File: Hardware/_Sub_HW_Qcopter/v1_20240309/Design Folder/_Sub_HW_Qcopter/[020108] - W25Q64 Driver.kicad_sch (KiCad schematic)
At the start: 3 parts, among them U2001 W25Q64JVSSIQ

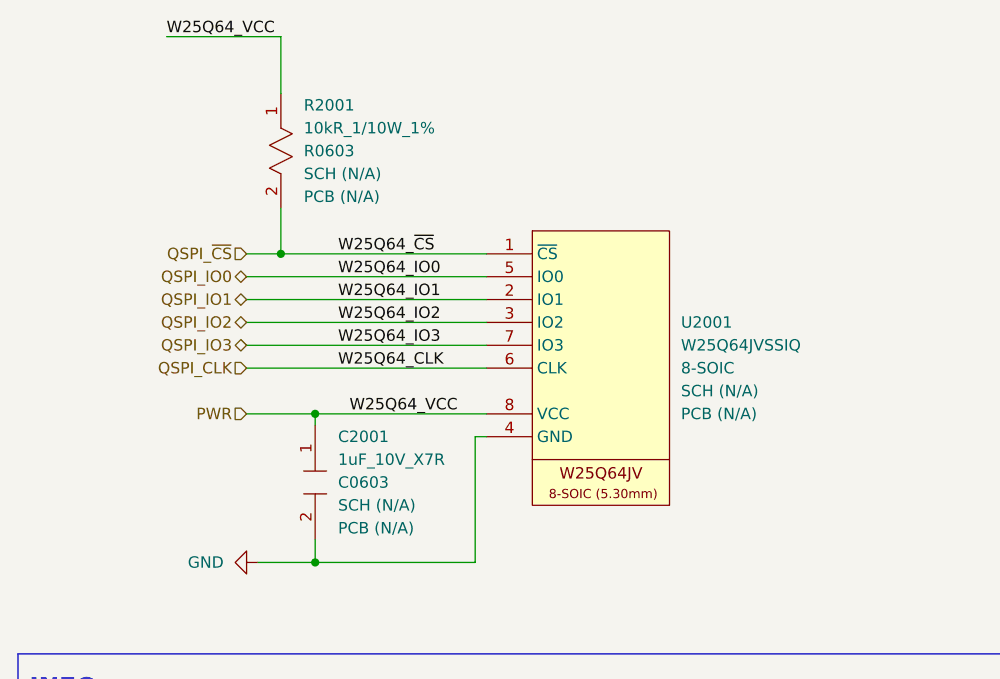
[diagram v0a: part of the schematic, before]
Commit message: Update [020108] - W25Q64 Driver.kicad_sch
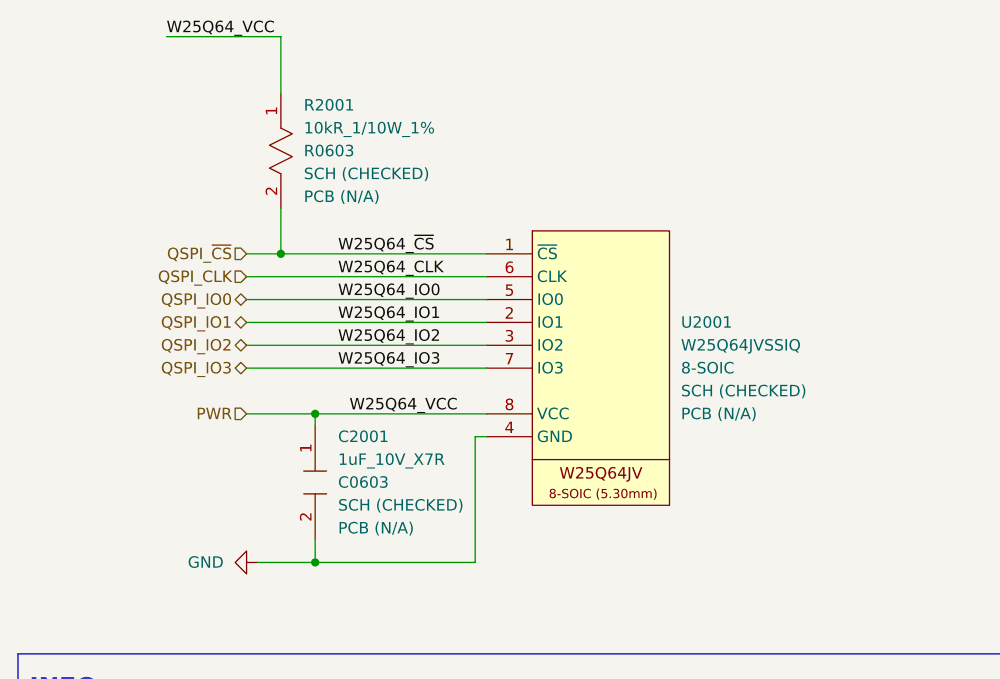
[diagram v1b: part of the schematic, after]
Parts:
- C2001, R2001, U2001: SCH CHECK SCH (N/A) -> SCH (CHECKED)
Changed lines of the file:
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@@
 	(wire
 		(pts
-			(xy 215.9 184.15) (xy 242.57 184.15)
+			(xy 215.9 186.69) (xy 242.57 186.69)
 		)
 		(stroke
@@
 	(wire
 		(pts
-			(xy 215.9 189.23) (xy 242.57 189.23)
+			(xy 215.9 179.07) (xy 242.57 179.07)
 		)
 		(stroke
@@
 	(wire
 		(pts
-			(xy 215.9 186.69) (xy 242.57 186.69)
+			(xy 215.9 189.23) (xy 242.57 189.23)
 		)
 		(stroke
@@
 	(wire
 		(pts
-			(xy 215.9 179.07) (xy 242.57 179.07)
+			(xy 215.9 181.61) (xy 242.57 181.61)
 		)
 		(stroke
@@
 	(wire
 		(pts
-			(xy 215.9 181.61) (xy 242.57 181.61)
+			(xy 215.9 184.15) (xy 242.57 184.15)
 		)
 		(stroke
@@
 	)
 	(label "W25Q64_IO2"
-		(at 226.06 184.15 0)
+		(at 226.06 186.69 0)
 		(fields_autoplaced yes)
 		(effects
@@
 	)
 	(label "W25Q64_IO1"
-		(at 226.06 181.61 0)
+		(at 226.06 184.15 0)
 		(fields_autoplaced yes)
 		(effects
@@
 	)
 	(label "W25Q64_IO3"
-		(at 226.06 186.69 0)
+		(at 226.06 189.23 0)
 		(fields_autoplaced yes)
 		(effects
@@
 	)
 	(label "W25Q64_CLK"
-		(at 226.06 189.23 0)
+		(at 226.06 179.07 0)
 		(fields_autoplaced yes)
 		(effects
@@
 	)
 	(label "W25Q64_IO0"
-		(at 226.06 179.07 0)
+		(at 226.06 181.61 0)
 		(fields_autoplaced yes)
 		(effects
@@
 	(hierarchical_label "QSPI_IO0"
 		(shape bidirectional)
-		(at 215.9 179.07 180)
+		(at 215.9 181.61 180)
 		(fields_autoplaced yes)
 		(effects
@@
 	(hierarchical_label "QSPI_IO3"
 		(shape bidirectional)
-		(at 215.9 186.69 180)
+		(at 215.9 189.23 180)
 		(fields_autoplaced yes)
 		(effects
@@
 	(hierarchical_label "QSPI_IO1"
 		(shape bidirectional)
-		(at 215.9 181.61 180)
+		(at 215.9 184.15 180)
 		(fields_autoplaced yes)
 		(effects
@@
 	(hierarchical_label "QSPI_IO2"
 		(shape bidirectional)
-		(at 215.9 184.15 180)
+		(at 215.9 186.69 180)
 		(fields_autoplaced yes)
 		(effects
@@
 	(hierarchical_label "QSPI_CLK"
 		(shape input)
-		(at 215.9 189.23 180)
+		(at 215.9 179.07 180)
 		(fields_autoplaced yes)
 		(effects
@@
 			)
 		)
-		(property "SCH CHECK" "SCH (N/A)"
+		(property "SCH CHECK" "SCH (CHECKED)"
 			(at 226.06 204.4699 90)
 			(effects
@@
 	)
 	(symbol
+		(lib_id "power:GND")
+		(at 217.17 210.82 270)
+		(unit 1)
+		(exclude_from_sim no)
+		(in_bom yes)
+		(on_board yes)
+		(dnp no)
+		(fields_autoplaced yes)
+		(property "Reference" "#PWR02001"
+			(at 210.82 210.82 0)
+			(effects
+				(font
+					(size 1.27 1.27)
+				)
+				(hide yes)
+			)
+		)
+		(property "Value" "GND"
+			(at 213.36 210.8199 90)
+			(effects
+				(font
+					(size 1.27 1.27)
+				)
+				(justify right)
+			)
+		)
+		(property "Footprint" ""
+			(at 217.17 210.82 0)
+			(effects
+				(font
+					(size 1.27 1.27)
+				)
+				(hide yes)
+			)
+		)
+		(property "Datasheet" ""
+			(at 217.17 210.82 0)
+			(effects
+				(font
+					(size 1.27 1.27)
+				)
+				(hide yes)
+			)
+		)
+		(property "Description" "Power symbol creates a global label with name \"GND\" , ground"
+			(at 217.17 210.82 0)
+			(effects
+				(font
+					(size 1.27 1.27)
+				)
+				(hide yes)
+			)
+		)
+		(pin "1"
+		)
+		(instances
+			(project "_Sub_HW_Qcopter"
+				(path "/b8703f06-b3da-4de2-b217-f104939b36e8/6184e84e-040e-4878-8152-76cf0b949e21/e826979f-4a88-401c-bba5-a1c30231907a/e9fb8b8e-a3bc-42c8-a6f2-2206c944e574"
+					(reference "#PWR02001")
+					(unit 1)
+				)
+			)
+		)
+	)
+	(symbol
 		(lib_id "_SCHLIB_Qcopter:IC_MEM_W25Q64JVSSIQ_64MBIT_NOR_QSPI/SPI_8-SOIC")
 		(at 247.65 173.99 0)
@@
 			)
 		)
-		(property "SCH CHECK" "SCH (N/A)"
+		(property "SCH CHECK" "SCH (CHECKED)"
 			(at 264.16 191.7699 0)
 			(effects
@@
 			)
 		)
+		(pin "4"
+		)
 		(pin "7"
 		)
@@
 		(pin "2"
 		)
-		(pin "4"
+		(pin "5"
+		)
+		(pin "1"
 		)
 		(pin "3"
@@
 		(pin "6"
 		)
-		(pin "1"
-		)
-		(pin "5"
-		)
 		(instances
 			(project "_Sub_HW_Qcopter"
@@
 	)
 	(symbol
-		(lib_id "power:GND")
-		(at 217.17 210.82 270)
-		(unit 1)
-		(exclude_from_sim no)
-		(in_bom yes)
-		(on_board yes)
-		(dnp no)
-		(fields_autoplaced yes)
-		(property "Reference" "#PWR02001"
-			(at 210.82 210.82 0)
-			(effects
-				(font
-					(size 1.27 1.27)
-				)
-				(hide yes)
-			)
-		)
-		(property "Value" "GND"
-			(at 213.36 210.8199 90)
-			(effects
-				(font
-					(size 1.27 1.27)
-				)
-				(justify right)
-			)
-		)
-		(property "Footprint" ""
-			(at 217.17 210.82 0)
-			(effects
-				(font
-					(size 1.27 1.27)
-				)
-				(hide yes)
-			)
-		)
-		(property "Datasheet" ""
-			(at 217.17 210.82 0)
-			(effects
-				(font
-					(size 1.27 1.27)
-				)
-				(hide yes)
-			)
-		)
-		(property "Description" "Power symbol creates a global label with name \"GND\" , ground"
-			(at 217.17 210.82 0)
-			(effects
-				(font
-					(size 1.27 1.27)
-				)
-				(hide yes)
-			)
-		)
-		(pin "1"
-		)
-		(instances
-			(project "_Sub_HW_Qcopter"
-				(path "/b8703f06-b3da-4de2-b217-f104939b36e8/6184e84e-040e-4878-8152-76cf0b949e21/e826979f-4a88-401c-bba5-a1c30231907a/e9fb8b8e-a3bc-42c8-a6f2-2206c944e574"
-					(reference "#PWR02001")
-					(unit 1)
-				)
-			)
-		)
-	)
-	(symbol
 		(lib_id "_SCHLIB_Qcopter:RES_10kR_1/10W_1%_R0603")
 		(at 219.71 158.75 270)
@@
 			)
 		)
-		(property "SCH CHECK" "SCH (N/A)"
+		(property "SCH CHECK" "SCH (CHECKED)"
 			(at 222.25 167.6399 90)
 			(effects
